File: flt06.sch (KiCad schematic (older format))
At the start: 28 parts

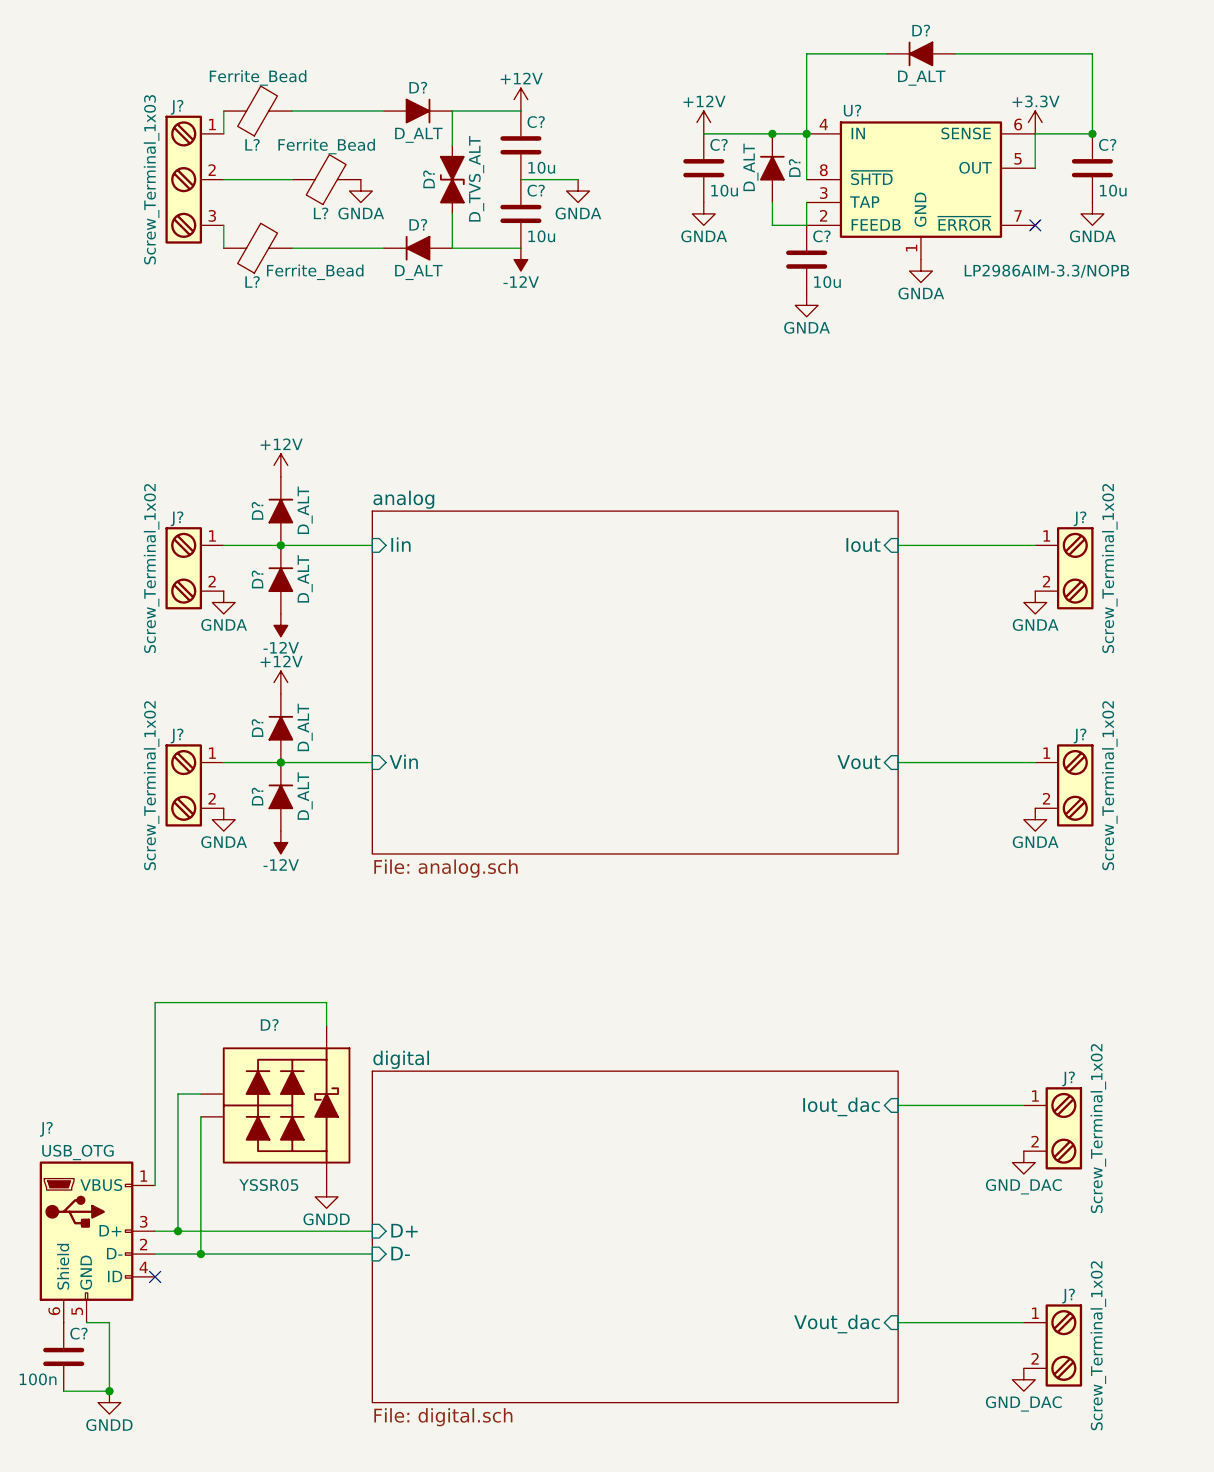
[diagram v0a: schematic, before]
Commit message: [sch] use an off-the-shelf pyboard to handle the digital part
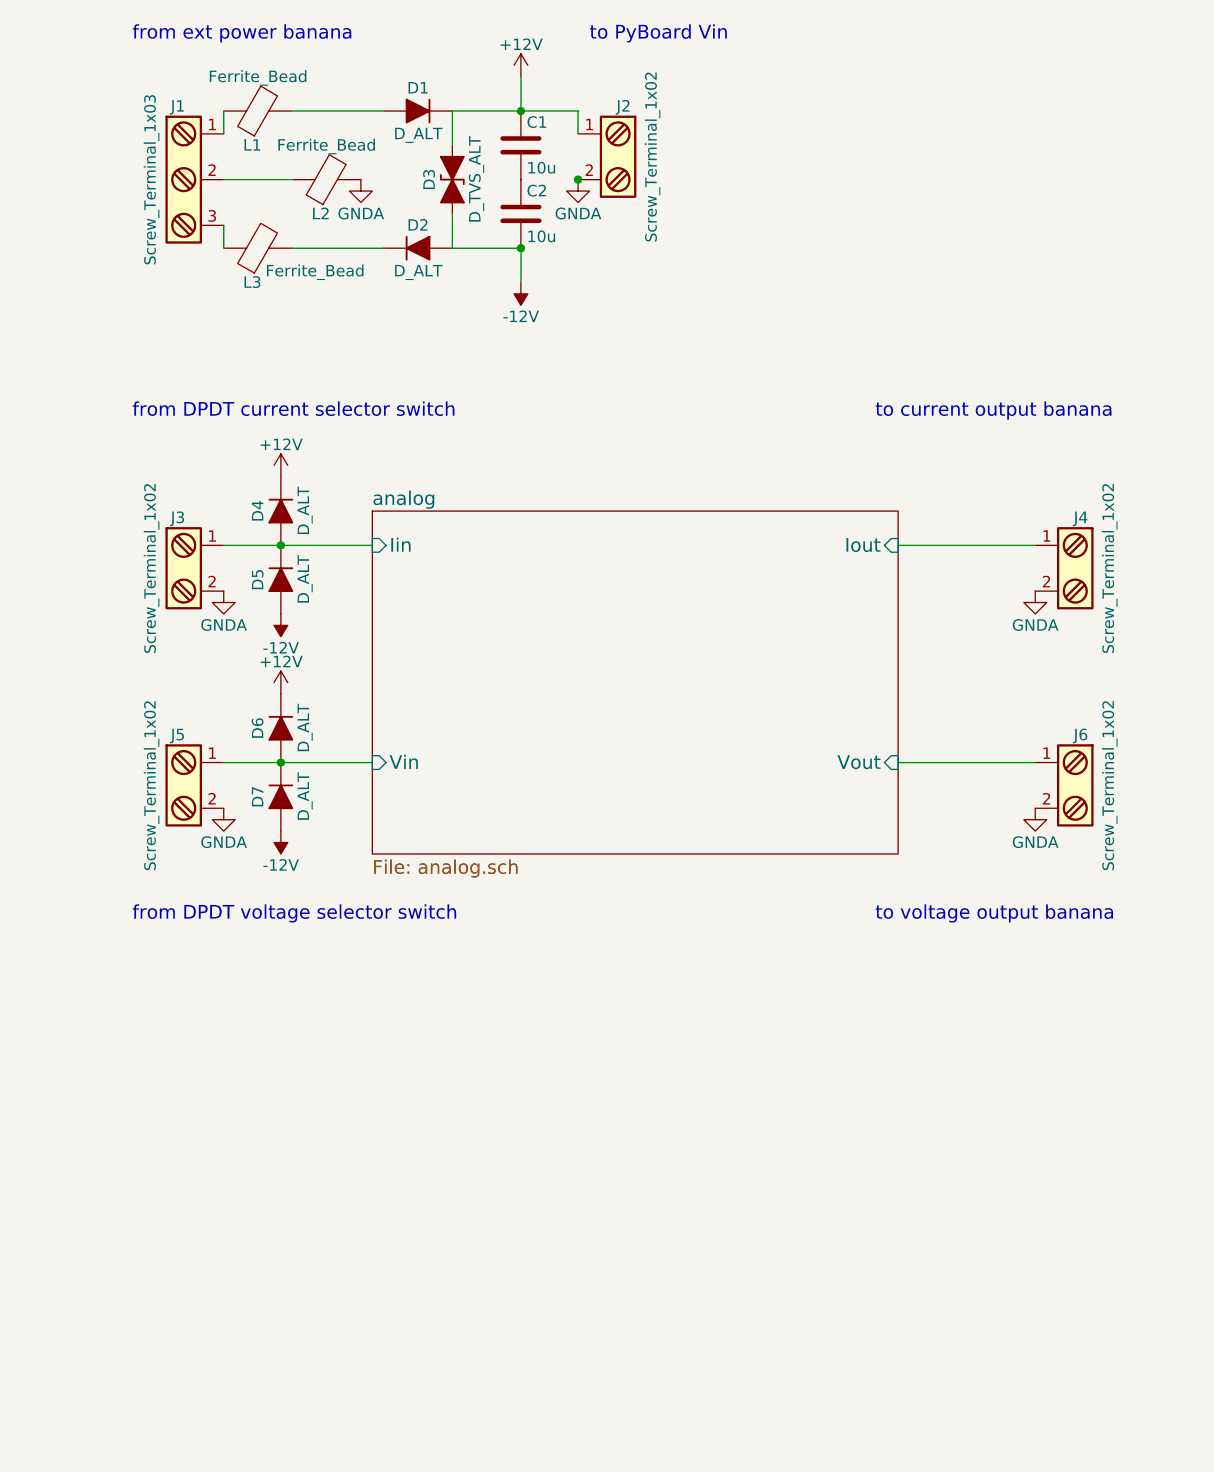
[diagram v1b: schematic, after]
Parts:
- removed C?: 100n, symbol C
- removed C? (x3): 10u, symbol C
- removed D?: YSSR05, symbol YSSR05
- removed D? (x2): D_ALT, symbol D_ALT
- removed J? (x2): Screw_Terminal_1x02, symbol Screw_Terminal_1x02
- removed J?: USB_OTG, symbol USB_OTG
- removed U?: LP2986AIM-3.3/NOPB, Housings_SOIC:SOIC-8_3.9x4.9mm_Pitch1.27mm, symbol LP2986AIM-3.3/NOPB
- added J2: Screw_Terminal_1x02, symbol Screw_Terminal_1x02
- gave numbers to parts that had none: 17
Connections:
- net +12V: now also J2.1
- net GNDA: now also J2.2; no longer C1.2, C2.1
- new net: C1.2, C2.1
- no-connect marks 2 -> 0
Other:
- note added: "from DPDT current selector switch"
- note added: "from DPDT voltage selector switch"
- note added: "from ext power banana"
- note added: "to PyBoard Vin"
- note added: "to current output banana"
- note added: "to voltage output banana"

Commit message: [pcb] layout rev1
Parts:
- added J19, J20: Screw_Terminal_1x02, Connectors_Terminal_Blocks:TerminalBlock_Pheonix_PT-3.5mm_2pol, symbol Screw_Terminal_1x02
- added Q1: BSS138, TO_SOT_Packages_SMD:SOT-23, symbol BSS138
- C1, C2: footprint (none) -> Capacitors_SMD:C_1210
- D1, D2, D4, D5, D6, D7: value D_ALT -> STPS160A; footprint (none) -> Diodes_SMD:D_SMA
- D3: value D_TVS_ALT -> SMAJ30CA; footprint (none) -> Diodes_SMD:D_SMA
- J1: footprint (none) -> Connectors_Terminal_Blocks:TerminalBlock_Pheonix_PT-3.5mm_3pol
- J2, J3, J4, J5, J6: footprint (none) -> Connectors_Terminal_Blocks:TerminalBlock_Pheonix_PT-3.5mm_2pol
- L1, L2, L3: value Ferrite_Bead -> R6H-2.5T; footprint (none) -> Resistors_THT:R_Axial_DIN0617_L17.0mm_D6.0mm_P5.08mm_Vertical
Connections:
- net GNDA: now also C1.2, C2.1, J19.2
- new net: J19.1, Q1.1 (G)
- new net: J20.1, Q1.3 (D)
- new net: J20.2, Q1.2 (S)
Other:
- note added: "from pyboard GPIO"
- note added: "to OC output banana"
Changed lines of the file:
@@
 F 0 "J1" H 1950 1900 50  0000 C TNN
 F 1 "Screw_Terminal_1x03" V 1800 1550 50  0000 C TNN
-F 2 "" H 1950 1225 50  0001 C CNN
+F 2 "Connectors_Terminal_Blocks:TerminalBlock_Pheonix_PT-3.5mm_3pol" H 1950 1225 50  0001 C CNN
 F 3 "" H 1925 1650 50  0001 C CNN
 	1    1950 1550
@@
 F 0 "J3" H 1950 3500 50  0000 C TNN
 F 1 "Screw_Terminal_1x02" V 1800 3250 50  0000 C TNN
-F 2 "" H 1950 3025 50  0001 C CNN
+F 2 "Connectors_Terminal_Blocks:TerminalBlock_Pheonix_PT-3.5mm_2pol" H 1950 3025 50  0001 C CNN
 F 3 "" H 1925 3250 50  0001 C CNN
 	1    1950 3250
@@
 F 0 "J5" H 1950 4450 50  0000 C TNN
 F 1 "Screw_Terminal_1x02" V 1800 4200 50  0000 C TNN
-F 2 "" H 1950 3975 50  0001 C CNN
+F 2 "Connectors_Terminal_Blocks:TerminalBlock_Pheonix_PT-3.5mm_2pol" H 1950 3975 50  0001 C CNN
 F 3 "" H 1925 4200 50  0001 C CNN
 	1    1950 4200
@@
 F 0 "J4" H 5900 3500 50  0000 C TNN
 F 1 "Screw_Terminal_1x02" V 5750 3250 50  0000 C TNN
-F 2 "" H 5900 3025 50  0001 C CNN
+F 2 "Connectors_Terminal_Blocks:TerminalBlock_Pheonix_PT-3.5mm_2pol" H 5900 3025 50  0001 C CNN
 F 3 "" H 5875 3250 50  0001 C CNN
 	1    5900 3250
@@
 P 2300 1250
 F 0 "L1" V 2150 1275 50  0000 C CNN
-F 1 "Ferrite_Bead" V 2450 1250 50  0000 C CNN
-F 2 "" V 2230 1250 50  0001 C CNN
+F 1 "R6H-2.5T" V 2450 1250 50  0000 C CNN
+F 2 "Resistors_THT:R_Axial_DIN0617_L17.0mm_D6.0mm_P5.08mm_Vertical" V 2230 1250 50  0001 C CNN
 F 3 "" H 2300 1250 50  0001 C CNN
 	1    2300 1250
@@
 P 2600 1550
 F 0 "L2" V 2450 1575 50  0000 C CNN
-F 1 "Ferrite_Bead" V 2750 1550 50  0000 C CNN
-F 2 "" V 2530 1550 50  0001 C CNN
+F 1 "R6H-2.5T" V 2750 1550 50  0000 C CNN
+F 2 "Resistors_THT:R_Axial_DIN0617_L17.0mm_D6.0mm_P5.08mm_Vertical" V 2530 1550 50  0001 C CNN
 F 3 "" H 2600 1550 50  0001 C CNN
 	1    2600 1550
@@
 P 2300 1850
 F 0 "L3" V 2150 1875 50  0000 C CNN
-F 1 "Ferrite_Bead" V 2200 1600 50  0000 C CNN
-F 2 "" V 2230 1850 50  0001 C CNN
+F 1 "R6H-2.5T" V 2200 1600 50  0000 C CNN
+F 2 "Resistors_THT:R_Axial_DIN0617_L17.0mm_D6.0mm_P5.08mm_Vertical" V 2230 1850 50  0001 C CNN
 F 3 "" H 2300 1850 50  0001 C CNN
 	1    2300 1850
@@
 P 3000 1850
 F 0 "D2" H 3000 1950 50  0000 C CNN
-F 1 "D_ALT" H 3000 1750 50  0000 C CNN
-F 2 "" H 3000 1850 50  0001 C CNN
+F 1 "STPS160A" H 3050 1750 50  0000 C CNN
+F 2 "Diodes_SMD:D_SMA" H 3000 1850 50  0001 C CNN
 F 3 "" H 3000 1850 50  0001 C CNN
 	1    3000 1850
@@
 U 1 1 5933D2FE
 P 3000 1250
-F 0 "D1" H 3000 1350 50  0000 C CNN
-F 1 "D_ALT" H 3000 1150 50  0000 C CNN
-F 2 "" H 3000 1250 50  0001 C CNN
+F 0 "D1" H 3000 1150 50  0000 C CNN
+F 1 "STPS160A" H 2950 1350 50  0000 C CNN
+F 2 "Diodes_SMD:D_SMA" H 3000 1250 50  0001 C CNN
 F 3 "" H 3000 1250 50  0001 C CNN
 	1    3000 1250
@@
 P 3150 1550
 F 0 "D3" H 3150 1650 50  0000 C CNN
-F 1 "D_TVS_ALT" H 3150 1450 50  0000 C CNN
-F 2 "" H 3150 1550 50  0001 C CNN
+F 1 "SMAJ30CA" H 3150 1450 50  0000 C CNN
+F 2 "Diodes_SMD:D_SMA" H 3150 1550 50  0001 C CNN
 F 3 "" H 3150 1550 50  0001 C CNN
 	1    3150 1550
@@
 F 0 "J6" H 5900 4450 50  0000 C TNN
 F 1 "Screw_Terminal_1x02" V 5750 4200 50  0000 C TNN
-F 2 "" H 5900 3975 50  0001 C CNN
+F 2 "Connectors_Terminal_Blocks:TerminalBlock_Pheonix_PT-3.5mm_2pol" H 5900 3975 50  0001 C CNN
 F 3 "" H 5875 4200 50  0001 C CNN
 	1    5900 4200
@@
 P 2400 3000
 F 0 "D4" H 2400 3100 50  0000 C CNN
-F 1 "D_ALT" H 2400 2900 50  0000 C CNN
-F 2 "" H 2400 3000 50  0001 C CNN
+F 1 "STPS160A" H 2350 2900 50  0000 C CNN
+F 2 "Diodes_SMD:D_SMA" H 2400 3000 50  0001 C CNN
 F 3 "" H 2400 3000 50  0001 C CNN
 	1    2400 3000
@@
 P 2400 3300
 F 0 "D5" H 2400 3400 50  0000 C CNN
-F 1 "D_ALT" H 2400 3200 50  0000 C CNN
-F 2 "" H 2400 3300 50  0001 C CNN
+F 1 "STPS160A" H 2450 3200 50  0000 C CNN
+F 2 "Diodes_SMD:D_SMA" H 2400 3300 50  0001 C CNN
 F 3 "" H 2400 3300 50  0001 C CNN
 	1    2400 3300
@@
 P 2400 3950
 F 0 "D6" H 2400 4050 50  0000 C CNN
-F 1 "D_ALT" H 2400 3850 50  0000 C CNN
-F 2 "" H 2400 3950 50  0001 C CNN
+F 1 "STPS160A" H 2350 3850 50  0000 C CNN
+F 2 "Diodes_SMD:D_SMA" H 2400 3950 50  0001 C CNN
 F 3 "" H 2400 3950 50  0001 C CNN
 	1    2400 3950
@@
 P 2400 4250
 F 0 "D7" H 2400 4350 50  0000 C CNN
-F 1 "D_ALT" H 2400 4150 50  0000 C CNN
-F 2 "" H 2400 4250 50  0001 C CNN
+F 1 "STPS160A" H 2450 4150 50  0000 C CNN
+F 2 "Diodes_SMD:D_SMA" H 2400 4250 50  0001 C CNN
 F 3 "" H 2400 4250 50  0001 C CNN
 	1    2400 4250
@@
 F 0 "C1" H 3475 1500 50  0000 L CNN
 F 1 "10u" H 3475 1300 50  0000 L CNN
-F 2 "" H 3488 1250 50  0001 C CNN
+F 2 "Capacitors_SMD:C_1210" H 3488 1250 50  0001 C CNN
 F 3 "" H 3450 1400 50  0001 C CNN
 	1    3450 1400
@@
 F 0 "C2" H 3475 1800 50  0000 L CNN
 F 1 "10u" H 3475 1600 50  0000 L CNN
-F 2 "" H 3488 1550 50  0001 C CNN
+F 2 "Capacitors_SMD:C_1210" H 3488 1550 50  0001 C CNN
 F 3 "" H 3450 1700 50  0001 C CNN
 	1    3450 1700
@@
 F 0 "J2" H 3900 1700 50  0000 C TNN
 F 1 "Screw_Terminal_1x02" V 3750 1450 50  0000 C TNN
-F 2 "" H 3900 1225 50  0001 C CNN
+F 2 "Connectors_Terminal_Blocks:TerminalBlock_Pheonix_PT-3.5mm_2pol" H 3900 1225 50  0001 C CNN
 F 3 "" H 3875 1450 50  0001 C CNN
 	1    3900 1450
@@
 Wire Wire Line
 	3450 1100 3450 1250
+Wire Wire Line
+	3700 1550 3450 1550
+Connection ~ 3450 1550
+$Comp
+L Screw_Terminal_1x02 J19
+U 1 1 59B12CEF
+P 1950 5800
+F 0 "J19" H 1950 6050 50  0000 C TNN
+F 1 "Screw_Terminal_1x02" V 1800 5800 50  0000 C TNN
+F 2 "Connectors_Terminal_Blocks:TerminalBlock_Pheonix_PT-3.5mm_2pol" H 1950 5575 50  0001 C CNN
+F 3 "" H 1925 5800 50  0001 C CNN
+	1    1950 5800
+	1    0    0    -1
+$EndComp
+$Comp
+L Screw_Terminal_1x02 J20
+U 1 1 59B12D94
+P 3250 5800
+F 0 "J20" H 3250 6050 50  0000 C TNN
+F 1 "Screw_Terminal_1x02" V 3100 5800 50  0000 C TNN
+F 2 "Connectors_Terminal_Blocks:TerminalBlock_Pheonix_PT-3.5mm_2pol" H 3250 5575 50  0001 C CNN
+F 3 "" H 3225 5800 50  0001 C CNN
+	1    3250 5800
+	-1   0    0    -1
+$EndComp
+$Comp
+L GNDA #PWR010
+U 1 1 59B12E5C
+P 2150 5900
+F 0 "#PWR010" H 2150 5650 50  0001 C CNN
+F 1 "GNDA" H 2150 5750 50  0000 C CNN
+F 2 "" H 2150 5900 50  0001 C CNN
+F 3 "" H 2150 5900 50  0001 C CNN
+	1    2150 5900
+	1    0    0    -1
+$EndComp
+$Comp
+L BSS138 Q1
+U 1 1 59B12F09
+P 2350 5700
+F 0 "Q1" H 2550 5775 50  0000 L CNN
+F 1 "BSS138" H 2550 5700 50  0000 L CNN
+F 2 "TO_SOT_Packages_SMD:SOT-23" H 2550 5625 50  0001 L CIN
+F 3 "" H 2350 5700 50  0001 L CNN
+	1    2350 5700
+	1    0    0    -1
+$EndComp
+Wire Wire Line
+	2450 5900 3050 5900
+Wire Wire Line
+	2450 5500 3050 5500
+Wire Wire Line
+	3050 5500 3050 5700
+Text Notes 1750 6350 0    60   ~ 0
+from pyboard GPIO
+Text Notes 2850 6350 0    60   ~ 0
+to OC output banana
 $EndSCHEMATC
